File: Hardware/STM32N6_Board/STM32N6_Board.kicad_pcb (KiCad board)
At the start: 4 copper layers, 82 x 78.7 mm, 148 parts, among them J1 Conn_01x02_Pin, J10 BOOT0, J11 Conn_01x18_Socket, J12 Conn_01x18_Socket, J2 Conn_01x02_Pin, J3 Conn_01x08_Pin, J4 Conn_01x18_Pin, J5 Conn_01x18_Pin, J6 Conn_01x05_Pin, J7 SFW15R-2STE1LF, J8 12401832E402A, J9 BOOT1, SW2 SW_Push, U1 STM32N657I0H3Q, U10 STMPS2151STR, U11 IS42S16800F-7BL, U12 ECMF2-40A100N6, U13 ECMF2-40A100N6, U14 ECMF2-40A100N6, U2 SPX5205-ADJ, U3 SPX5205-ADJ, U4 SPX5205-ADJ, U5 SPX5205-ADJ, U6 MC34064-ADJ-TR, U7 MX25LM51245GXDI00, U8 SPX5205-ADJ, U9 ECMF2-40A100N6, Y1 32.768kHz, Y3 48MHz

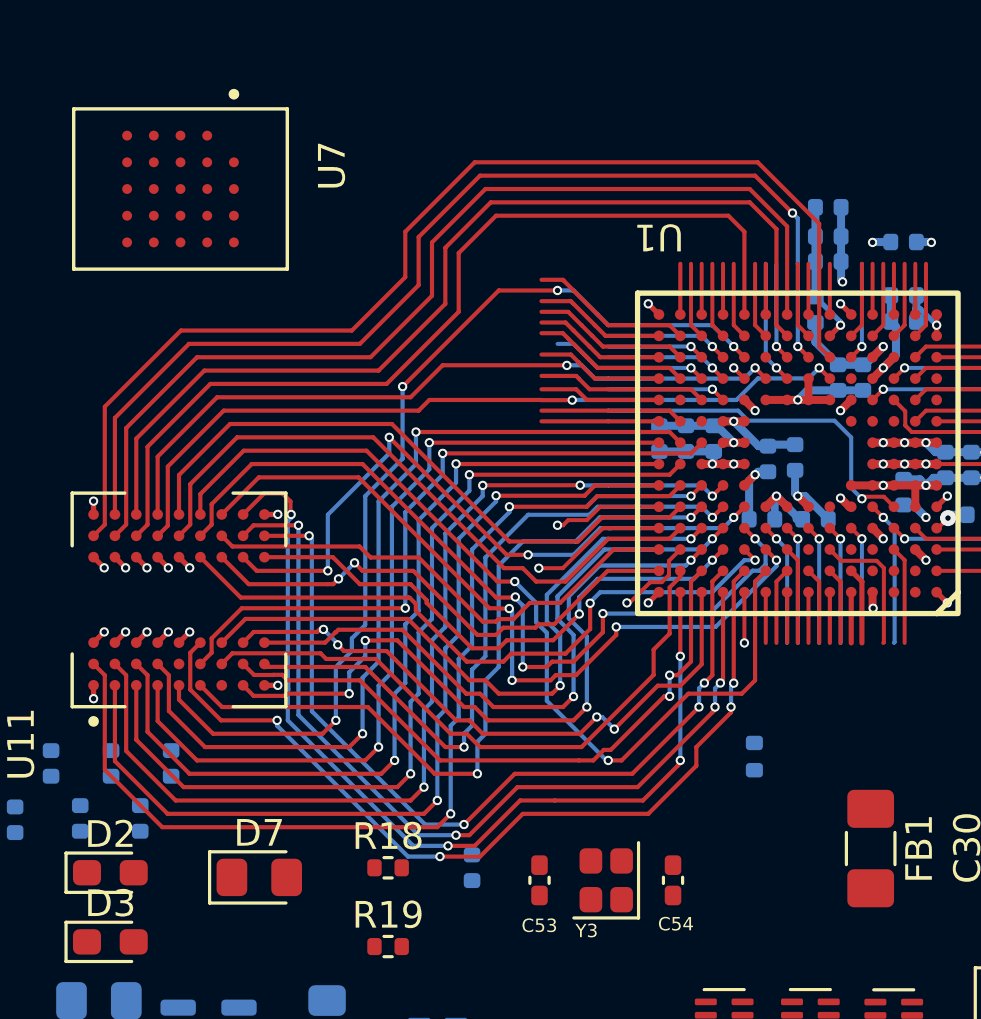
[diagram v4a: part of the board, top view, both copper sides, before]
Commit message: Finished the length matching.
- The SDRAM chip has no diff traces. So all to +-10mm of clock.
- Clock trace length is 34.2mm currently, so all are 24.2 -> 44.2
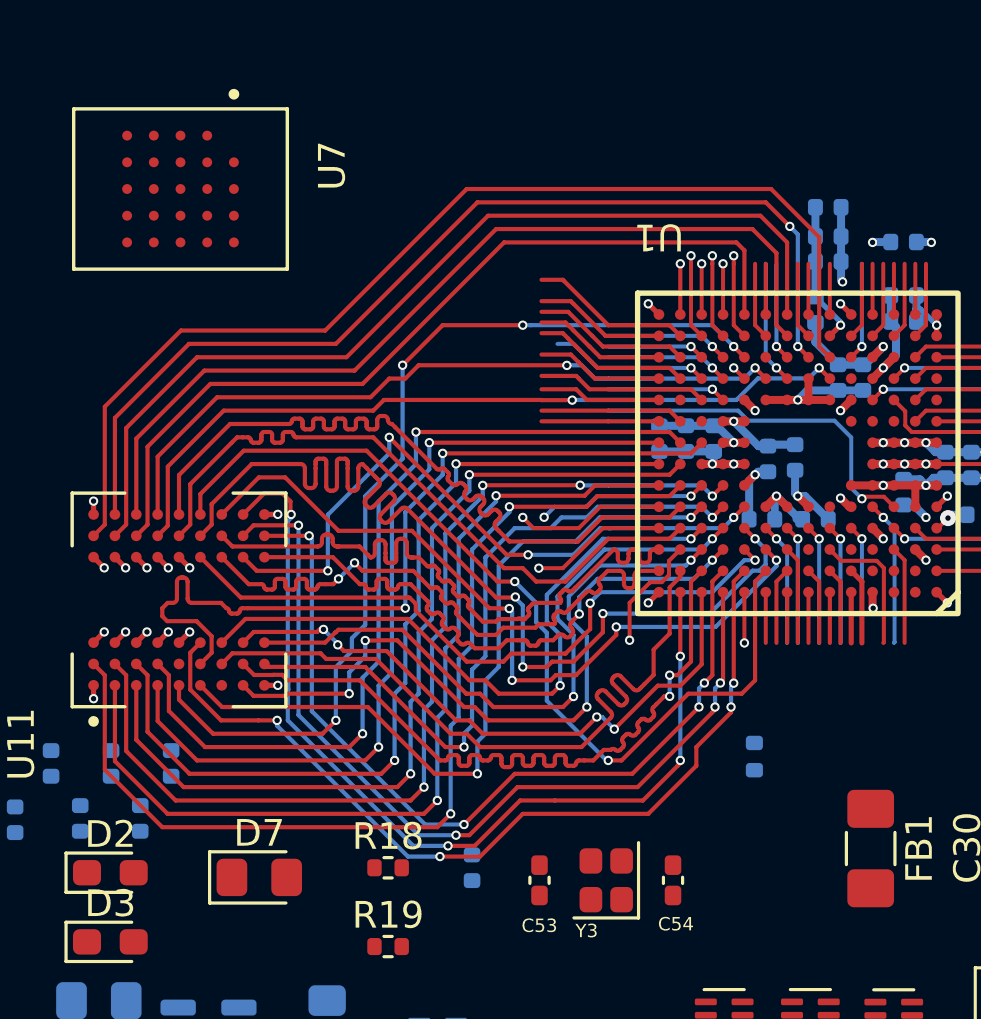
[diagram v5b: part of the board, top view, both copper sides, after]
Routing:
- net /FMC_SDRAM/FMC_SDNRAS: track 31.0 -> 40.2 mm
- net /FMC_SDRAM/FMC_SDCLK: track 25.1 -> 31.0 mm
- net /FMC_SDRAM/FMC_BA1: track 18.8 -> 24.5 mm
- net /FMC_SDRAM/FMC_D2: track 23.4 -> 28.0 mm
- net /FMC_SDRAM/FMC_A7: track 23.8 -> 27.9 mm
- net /FMC_SDRAM/FMC_BA0: track 19.2 -> 22.7 mm
- net /FMC_SDRAM/FMC_A11: track 23.2 -> 26.6 mm
- net /FMC_SDRAM/FMC_D5: track 36.3 -> 33.7 mm
- net /FMC_SDRAM/FMC_D7: track 34.1 -> 31.6 mm
- net /FMC_SDRAM/FMC_D4: track 37.7 -> 35.4 mm
- net /FMC_SDRAM/FMC_D3: track 40.0 -> 37.8 mm
- net /FMC_SDRAM/FMC_A3: track 20.6 -> 22.7 mm
- net /FMC_SDRAM/FMC_D1: track 42.7 -> 40.6 mm
- net /Connectors/USART3_RX: track 9.65 -> 11.4 mm, vias 1 -> 2
- net /Connectors/TIM4_CH2: track 9.09 -> 10.6 mm
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
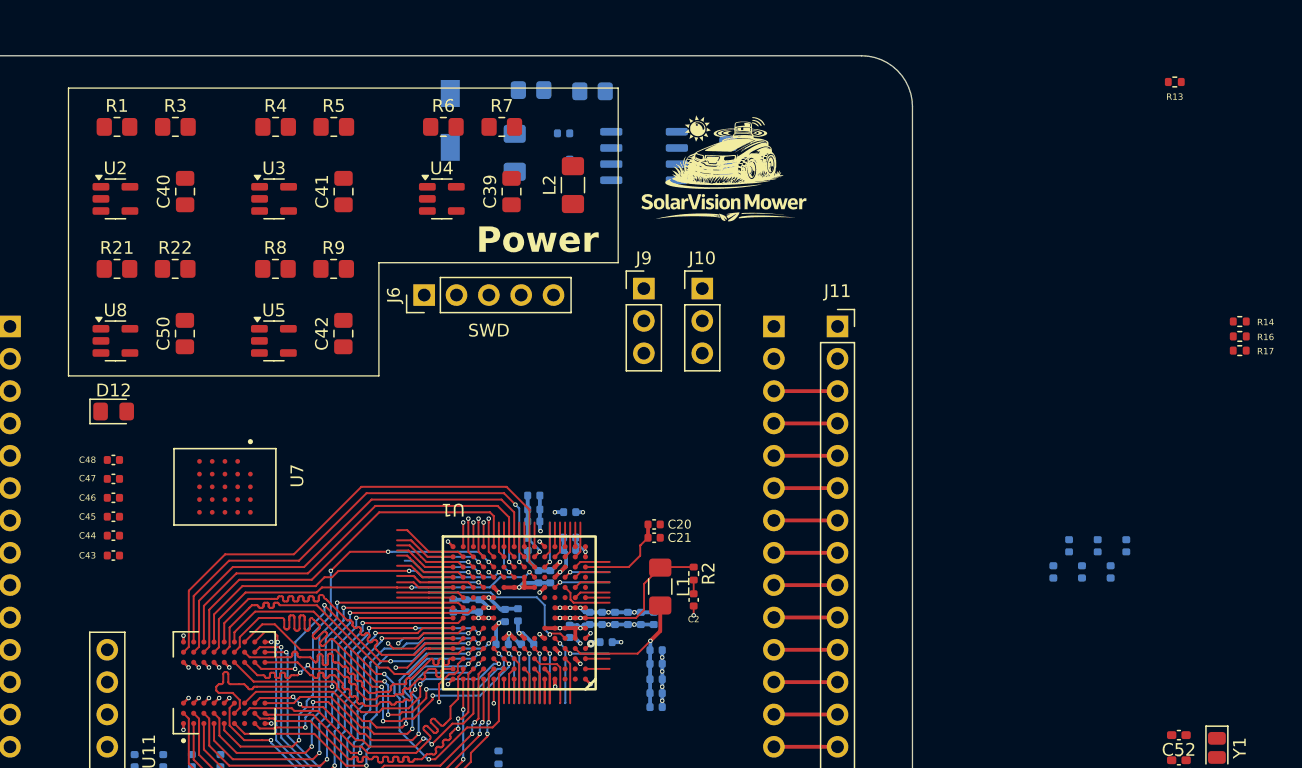
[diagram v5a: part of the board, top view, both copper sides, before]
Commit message: Fanned out and routed the MX25LM. Much easier.
- The NOR flash chip is now fanned out, routed, and bypass caps are
  placed.
- Still need bypass caps on the IS42S
- I also changed the SDRAM clock a little, to avoid a small loop.
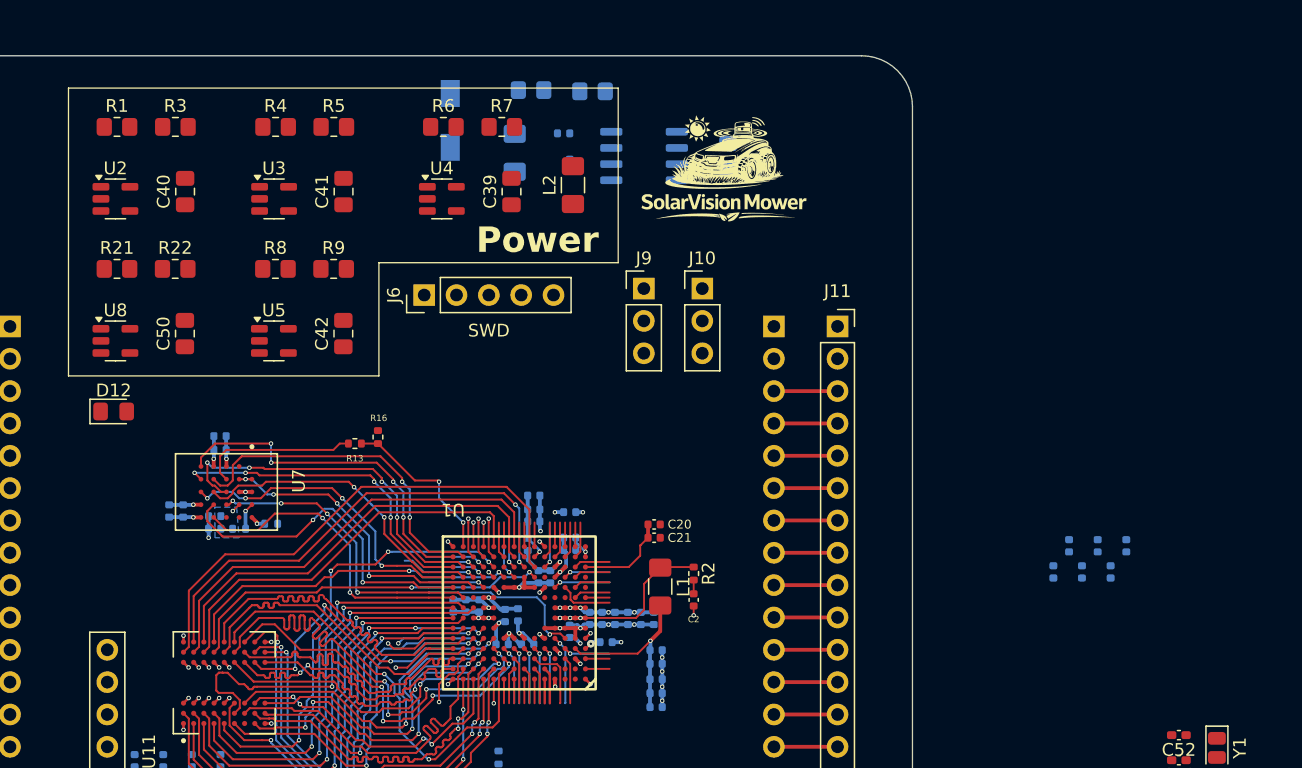
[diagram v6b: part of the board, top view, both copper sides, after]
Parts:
- C43, C44, C45, C46, C47, C48, R14, R17: moved to B.Cu
- moved R14 80.3 mm to (178.0, 115.9), turned to 180 degrees
- moved R17 77.3 mm to (180.5, 115.5)
- moved R13 70.4 mm to (187.1, 109.2)
- moved R16 68.2 mm to (188.9, 108.7), turned to 90 degrees
- moved C47 8.68 mm to (176.5, 109.7), turned to 0 degrees
- moved C48 8.58 mm to (176.5, 108.6), turned to 0 degrees
- moved C46 8.32 mm to (176.1, 115.9)
- moved C45 7.96 mm to (176.1, 114.9)
- moved C44 5.81 mm to (173.6, 114.5), turned to -90 degrees
- moved C43 5.61 mm to (172.5, 114.5), turned to -90 degrees
- moved U7 0.42 mm to (177.0, 113.0)
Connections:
- U7 pad A2: unconnected-(U7-NC-PadA2) -> /GPIO/PN6
- U7 pad A3: unconnected-(U7-NC-PadA3) -> GND
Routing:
- net /GPIO/PN0: track 5.90 -> 28.7 mm, vias 0 -> 4
- net /GPIO/PN11: track 4.94 -> 27.6 mm, vias 0 -> 4
- net /GPIO/PN5: track 4.57 -> 26.8 mm, vias 0 -> 2
- net /GPIO/PN10: track 4.94 -> 25.8 mm, vias 0 -> 4
- net /GPIO/PN3: track 6.07 -> 26.9 mm, vias 0 -> 2
- net /GPIO/PN8: track 4.40 -> 24.7 mm, vias 0 -> 2
- net /GPIO/PN9: track 4.77 -> 24.9 mm, vias 0 -> 4
- net /GPIO/PN4: track 5.37 -> 24.1 mm, vias 0 -> 4
- net /GPIO/PN2: track 5.90 -> 24.3 mm, vias 0 -> 2
- net /GPIO/PN6: track 6.37 -> 24.3 mm, vias 0 -> 4
- net Net-(U7-~{CS}): track 0.00 -> 12.5 mm
- net /GPIO/PN1: track 1.90 -> 13.2 mm, vias 1 -> 2
- net GND: track 43.2 -> 50.8 mm, vias 28 -> 32
- net /XSPI NOR Flash/VDD_OCTO: track 0.00 -> 5.63 mm, vias 0 -> 3
- net /Analog_Unit/NRST: track 5.45 -> 7.56 mm, vias 1 -> 2
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- added copper zone on B.Cu, net /XSPI NOR Flash/VDD_OCTO
